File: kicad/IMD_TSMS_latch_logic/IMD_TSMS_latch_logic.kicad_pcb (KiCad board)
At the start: 2 copper layers, 32 parts, among them IC1 NE555, Q2 Q_PMOS_GDS, Q3 Q_PMOS_GDS, SW1 SW_Push, U1 4001, U2 4009, U3 4009, U4 4001

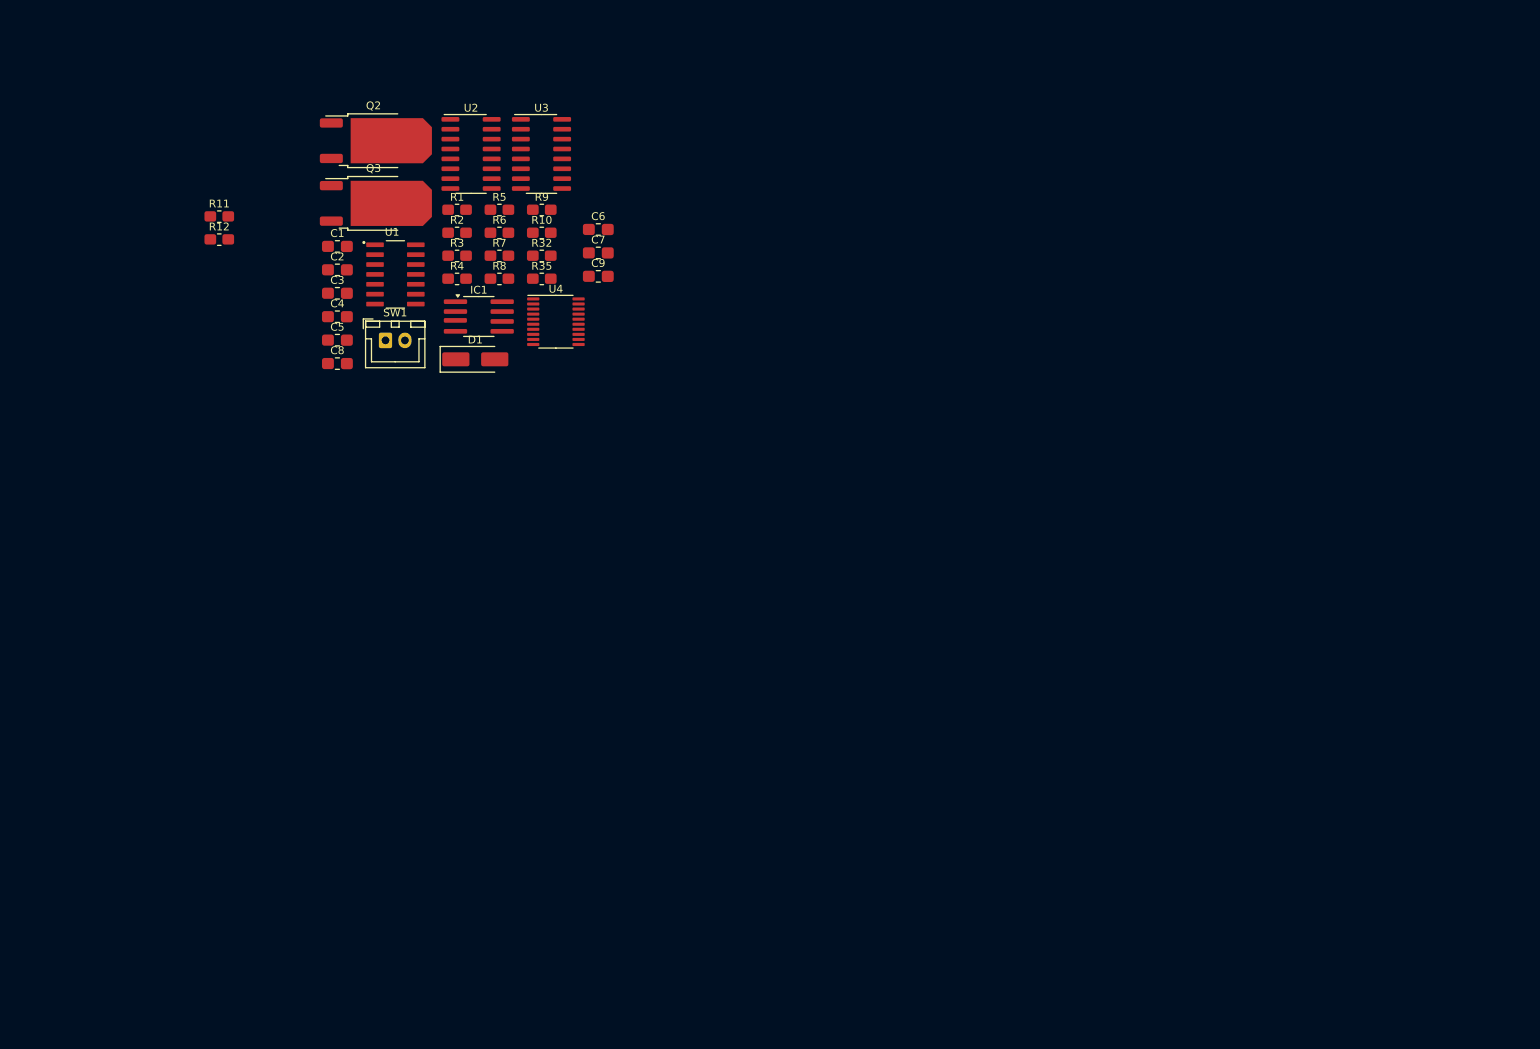
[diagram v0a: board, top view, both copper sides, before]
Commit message: Draw IMD latch
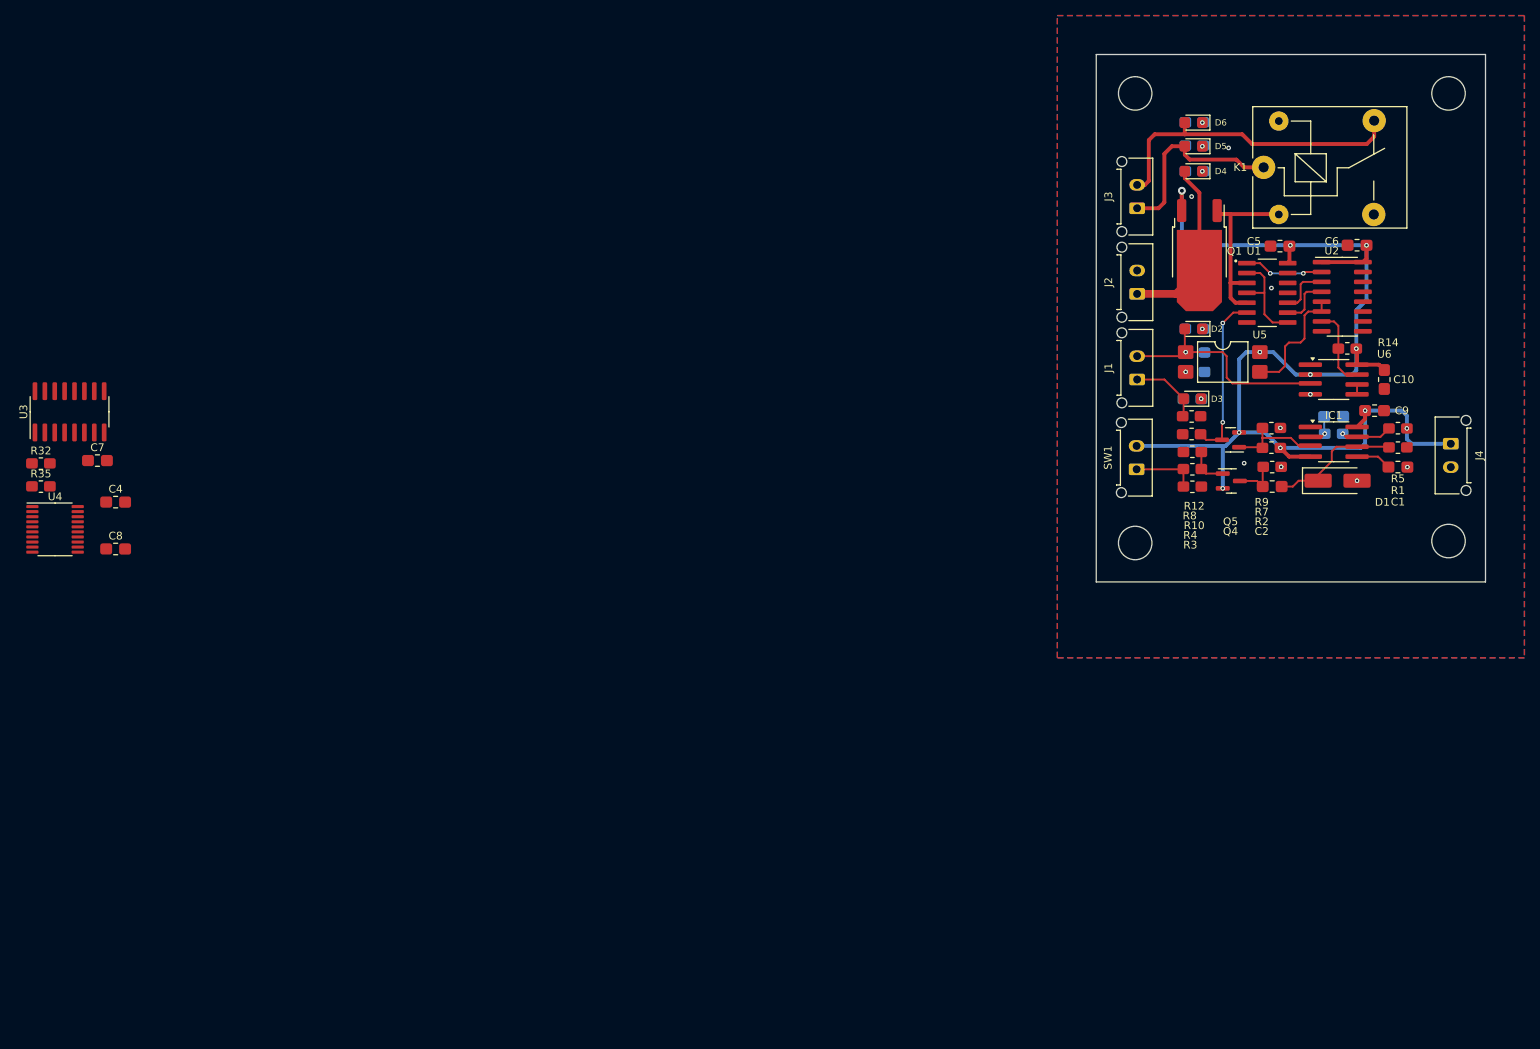
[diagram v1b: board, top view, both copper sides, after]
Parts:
- removed Q2, Q3: Q_PMOS_GDS, RMC_TO:TO-252-2
- added C10: 100nF, RMC_Capacitor:C_0805_2012Metric_Pad1.18x1.45mm_HandSolder_L, F.Cu at (187.0, 61.8)
- added D2: LED, RMC_LED:LED_0805_2012Metric_Pad1.45x1.40mm_HandSolder, F.Cu at (162.5, 55.2)
- added D3: LED, RMC_LED:LED_0805_2012Metric_Pad1.45x1.40mm_HandSolder, F.Cu at (162.3, 64.2)
- added D4: LED, RMC_LED:LED_0805_2012Metric_Pad1.45x1.40mm_HandSolder, F.Cu at (162.5, 35.0)
- added D5: LED, RMC_LED:LED_0805_2012Metric_Pad1.45x1.40mm_HandSolder, F.Cu at (162.5, 31.8)
- added D6: LED, RMC_LED:LED_0805_2012Metric_Pad1.45x1.40mm_HandSolder, F.Cu at (162.5, 28.8)
- added H1: MountingHole, MountingHole:MountingHole_4.3mm_M4, F.Cu at (195.2, 25.0)
- added H2: MountingHole, MountingHole:MountingHole_4.3mm_M4, F.Cu at (195.2, 82.5)
- added H3: MountingHole, MountingHole:MountingHole_4.3mm_M4, F.Cu at (155.0, 82.8)
- added H4: MountingHole, MountingHole:MountingHole_4.3mm_M4, F.Cu at (155.0, 25.0)
- added J1: Conn_01x02, Connector_Molex:Molex_Micro-Fit_3.0_43650-0215_1x02_P3.00mm_Vertical, F.Cu at (155.2, 61.8)
- added J2: Conn_01x02, Connector_Molex:Molex_Micro-Fit_3.0_43650-0215_1x02_P3.00mm_Vertical, F.Cu at (155.2, 50.8)
- added J3: Conn_01x02, Connector_Molex:Molex_Micro-Fit_3.0_43650-0215_1x02_P3.00mm_Vertical, F.Cu at (155.2, 39.8)
- added J4: Conn_01x02, Connector_Molex:Molex_Micro-Fit_3.0_43650-0215_1x02_P3.00mm_Vertical, F.Cu at (195.5, 70.0)
- added K1: SANYOU_SRD_Form_C, Relay_THT:Relay_SPDT_SANYOU_SRD_Series_Form_C, F.Cu at (171.5, 34.5)
- added Q1: Q_PMOS_GDS, RMC_TO:TO-252-2, F.Cu at (163.2, 45.5)
- added Q4: AO3401A, RMC_SOT:SOT-23, F.Cu at (167.3, 74.8)
- added Q5: AO3401A, RMC_SOT:SOT-23, F.Cu at (167.2, 69.5)
- added R13: 1k, RMC_Resistor:R_0805_2012Metric_Pad1.20x1.40mm_HandSolder_L, B.Cu at (162.8, 60.8)
- added R14: 1k, RMC_Resistor:R_0805_2012Metric_Pad1.20x1.40mm_HandSolder_L, F.Cu at (182.2, 57.8)
- added R15: 1k, RMC_Resistor:R_0805_2012Metric_Pad1.20x1.40mm_HandSolder_L, B.Cu at (162.6, 55.2)
- added R16: 1k, RMC_Resistor:R_0805_2012Metric_Pad1.20x1.40mm_HandSolder_L, B.Cu at (162.3, 64.2)
- added R17: 1k, RMC_Resistor:R_0805_2012Metric_Pad1.20x1.40mm_HandSolder_L, B.Cu at (162.6, 35.0)
- added R18: 1k, RMC_Resistor:R_0805_2012Metric_Pad1.20x1.40mm_HandSolder_L, B.Cu at (162.6, 31.7)
- added R19: 1k, RMC_Resistor:R_0805_2012Metric_Pad1.20x1.40mm_HandSolder_L, B.Cu at (162.6, 28.7)
- added U5: LTV-817S, Package_DIP:SMDIP-4_W9.53mm, F.Cu at (166.2, 59.5)
- added U6: LM311, RMC_SO:SOIC-8_3.9x4.9mm_P1.27mm_RMC_Handsolder, F.Cu at (180.5, 61.8)
- C3, R11, R6: moved to B.Cu
- SW1: footprint Connector_JST:JST_XH_B2B-XH-A_1x02_P2.50mm_Vertical -> Connector_Molex:Molex_Micro-Fit_3.0_43650-0215_1x02_P3.00mm_Vertical
- moved C1 139.1 mm to (188.8, 73.0)
- moved C3 129.0 mm to (180.5, 66.5)
- moved R12 127.0 mm to (162.2, 66.5)
- moved R11 126.6 mm to (162.8, 58.2)
- moved R1 124.7 mm to (188.8, 70.5)
- moved C2 123.3 mm to (172.6, 75.5)
- moved C5 121.7 mm to (173.6, 44.6), turned to 180 degrees
- moved R5 118.8 mm to (188.8, 68.0), turned to 180 degrees
- moved U2 113.4 mm to (181.6, 51.1)
- moved U1 112.0 mm to (172.0, 50.6)
- moved D1 111.9 mm to (181.0, 74.8)
- moved IC1 111.0 mm to (180.5, 69.8)
- moved R6 110.2 mm to (180.5, 68.8), turned to 180 degrees
- moved R2 108.9 mm to (172.6, 73.0)
- moved R7 102.2 mm to (172.5, 70.5), turned to 180 degrees
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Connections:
- net /IMD_latch_output renamed Net-(U1-Pad2)
- net Net-(U1-Pad3) renamed IMD_RELAY
- R12 pad 1: IMD_MHs -> /IMD_MHs
- U2 pad 5: /IMD_OKHs -> /OKHs_logic
- U2 pad 6: unconnected-(U2-Pad6) -> /OKHs_logic
- U2 pad 7: unconnected-(U2-Pad7) -> Net-(R14-Pad2)
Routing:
- net +12V: track 0.00 -> 153.7 mm, vias 0 -> 11
- net /SDC_OUT: track 0.00 -> 40.7 mm
- net /IMD_OKHs: track 0.00 -> 28.9 mm, vias 0 -> 1
- net IMD_LED: track 0.00 -> 25.1 mm
- net /SDC_IN: track 0.00 -> 25.0 mm
- net IMD_RELAY: track 0.00 -> 24.6 mm
- net /IMD_reset: track 0.00 -> 21.7 mm, vias 0 -> 2
- net /THRES: track 0.00 -> 17.1 mm
- net /OKHs_logic: track 0.00 -> 15.6 mm
- net Net-(U1-Pad2): track 0.00 -> 12.9 mm
- net /fall_edge_out: track 0.00 -> 12.2 mm
- net Net-(R14-Pad2): track 0.00 -> 10.5 mm
- net Net-(U1-Pad1): track 0.00 -> 10.2 mm, vias 0 -> 2
- net /IMD_MHs: track 0.00 -> 9.30 mm
- net Net-(R3-Pad1): track 0.00 -> 8.28 mm
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- added copper zone on B.Cu, net GND
- added copper zone on F.Cu, net GND
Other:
- board outline added: 50 x 67.8 mm

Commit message: IMD latch with small IMD moutning
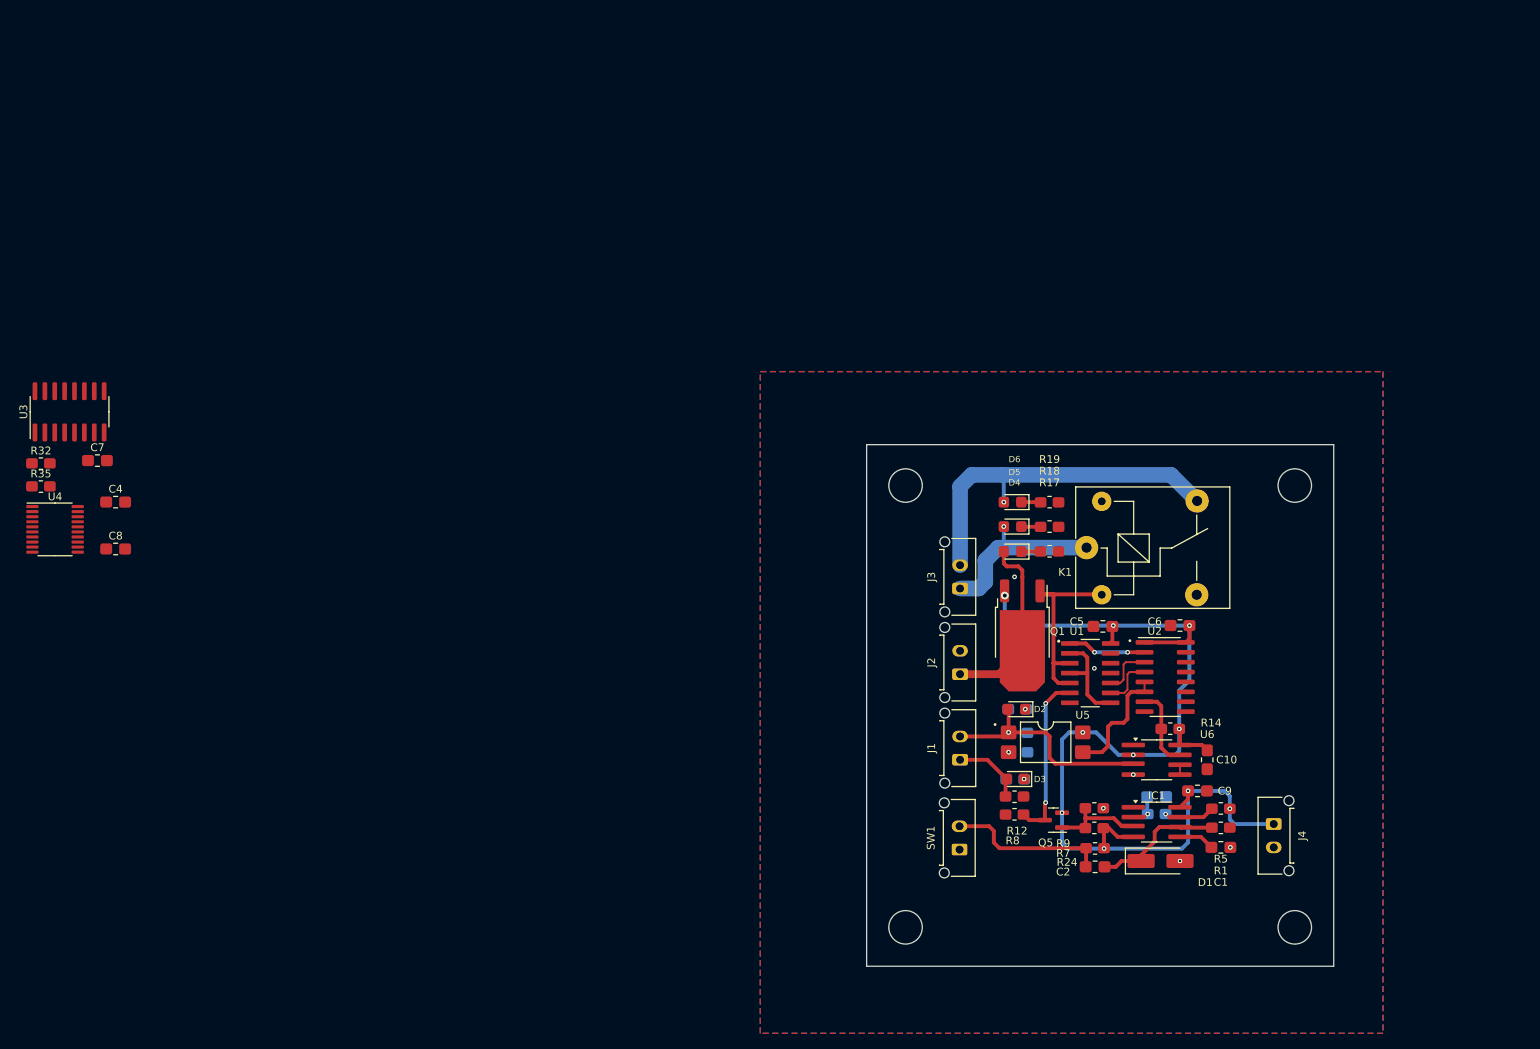
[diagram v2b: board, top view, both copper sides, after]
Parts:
- removed Q4: AO3401A, RMC_SOT:SOT-23
- removed R10: 100k, RMC_Resistor:R_0805_2012Metric_Pad1.20x1.40mm_HandSolder_L
- removed R2: 10k, RMC_Resistor:R_0805_2012Metric_Pad1.20x1.40mm_HandSolder_L
- removed R3, R4: 1k, RMC_Resistor:R_0805_2012Metric_Pad1.20x1.40mm_HandSolder_L
- added R24: 10k, RMC_Resistor:R_0805_2012Metric_Pad1.20x1.40mm_HandSolder_L, F.Cu at (149.8, 122.0)
- R17, R18, R19: moved to F.Cu
- moved H1 108.9 mm to (175.5, 132.1), turned to -90 degrees
- moved H2 85.6 mm to (125.5, 132.1), turned to -90 degrees
- moved H4 54.4 mm to (175.5, 75.4), turned to -90 degrees
- moved D5 54.1 mm to (139.2, 80.6)
- moved D4 54.1 mm to (139.2, 83.8)
- moved D6 54.0 mm to (139.2, 77.5)
- moved C5 53.9 mm to (150.9, 93.5)
- moved U1 53.9 mm to (149.2, 99.5)
- moved U2 53.9 mm to (158.9, 100.0)
- moved C1 53.9 mm to (166.0, 121.8)
- moved C10 53.9 mm to (164.3, 110.6)
- moved C2 53.9 mm to (149.9, 124.3)
- moved C3 53.9 mm to (157.8, 115.3)
- moved C6 53.9 mm to (160.8, 93.3)
- moved C9 53.9 mm to (163.0, 114.6)
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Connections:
- C2 pad 1: Net-(Q4-D) -> Net-(C2-Pad1)
- SW1 pad 1: Net-(R3-Pad1) -> GND
- SW1 pad 2: +12V -> Net-(C2-Pad1)
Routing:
- net Net-(C2-Pad1): track 0.00 -> 20.7 mm
- net +12V: track 153.7 -> 137.2 mm, vias 11 -> 10
- net Net-(R3-Pad1): track 8.28 -> 0.00 mm
- net Net-(Q4-D): track 5.78 -> 0.00 mm
- net /SDC_OUT: track 40.7 -> 46.1 mm, vias 0 -> 1
- net Net-(Q4-G): track 5.17 -> 0.00 mm
- net /fall_edge_out: track 12.2 -> 14.7 mm
- net Net-(D4-K): track 0.12 -> 2.47 mm, vias 1 -> 0
- net Net-(D6-K): track 0.14 -> 2.49 mm, vias 1 -> 0
- net Net-(D5-K): track 0.16 -> 2.49 mm, vias 1 -> 0
- net /SDC_IN: track 25.0 -> 22.8 mm, vias 0 -> 1
- net IMD_LED: track 25.1 -> 23.9 mm
- net GND: vias 9 -> 6
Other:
- board size 50 x 67.8 mm -> 60 x 67 mm

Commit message: did all 3 boards
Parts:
- removed J2: Conn_01x02, Connector_Molex:Molex_Micro-Fit_3.0_43650-0215_1x02_P3.00mm_Vertical
- removed Q1: Q_PMOS_GDS, RMC_TO:TO-252-2
- added D7: LED, RMC_LED:LED_0805_2012Metric_Pad1.45x1.40mm_HandSolder, F.Cu at (92.8, 85.7)
- added H10: MountingHole, MountingHole:MountingHole_4.3mm_M4, F.Cu at (115.0, 75.4)
- added H11: MountingHole, MountingHole:MountingHole_4.3mm_M4, F.Cu at (80.0, 85.0)
- added H12: MountingHole, MountingHole:MountingHole_4.3mm_M4, F.Cu at (115.0, 85.0)
- added H5: MountingHole, MountingHole:MountingHole_4.3mm_M4, F.Cu at (115.0, 132.0)
- added H6: MountingHole, MountingHole:MountingHole_4.3mm_M4, F.Cu at (115.0, 96.0)
- added H7: MountingHole, MountingHole:MountingHole_4.3mm_M4, F.Cu at (80.0, 132.0)
- added H8: MountingHole, MountingHole:MountingHole_4.3mm_M4, F.Cu at (80.0, 75.4)
- added H9: MountingHole, MountingHole:MountingHole_4.3mm_M4, F.Cu at (80.0, 96.0)
- added J5: Conn_01x02, Connector_Molex:Molex_Micro-Fit_3.0_43650-0215_1x02_P3.00mm_Vertical, F.Cu at (90.8, 78.0)
- added J6: Conn_01x02, Connector_Molex:Molex_Micro-Fit_3.0_43650-0215_1x02_P3.00mm_Vertical, F.Cu at (102.0, 78.0)
- added J7: Conn_01x02, Connector_Molex:Molex_Micro-Fit_3.0_43650-0215_1x02_P3.00mm_Vertical, F.Cu at (132.5, 99.8)
- added J8: Conn_01x02, Connector_Molex:Molex_Micro-Fit_3.0_43650-0215_1x02_P3.00mm_Vertical, F.Cu at (106.4, 114.5)
- added J9: Conn_01x02, Connector_Molex:Molex_Micro-Fit_3.0_43650-0215_1x02_P3.00mm_Vertical, F.Cu at (106.4, 125.8)
- added K2: SANYOU_SRD_Form_C, Relay_THT:Relay_SPDT_SANYOU_SRD_Series_Form_C, F.Cu at (93.5, 114.0)
- added Q2: AO3400A, RMC_SOT:SOT-23, F.Cu at (98.0, 84.2)
- added Q3: AO3401A, RMC_SOT:SOT-23, F.Cu at (90.2, 106.6)
- added Q6: AO3401A, RMC_SOT:SOT-23, F.Cu at (139.8, 96.2)
- added R10: 100k, RMC_Resistor:R_0805_2012Metric_Pad1.20x1.40mm_HandSolder_L, F.Cu at (139.8, 101.5)
- added R2: 1k, RMC_Resistor:R_0805_2012Metric_Pad1.20x1.40mm_HandSolder_L, F.Cu at (154.8, 106.8)
- added R20: 1k, RMC_Resistor:R_0805_2012Metric_Pad1.20x1.40mm_HandSolder_L, F.Cu at (104.2, 84.7)
- added R21: 1k, RMC_Resistor:R_0805_2012Metric_Pad1.20x1.40mm_HandSolder_L, F.Cu at (92.8, 83.2)
- added R22: JUMPER, RMC_Resistor:R_0805_2012Metric_Pad1.20x1.40mm_HandSolder_L, F.Cu at (145.2, 89.2)
- added R23: 1k, RMC_Resistor:R_0805_2012Metric_Pad1.20x1.40mm_HandSolder_L, F.Cu at (149.8, 116.8)
- added R25: 1k, RMC_Resistor:R_0805_2012Metric_Pad1.20x1.40mm_HandSolder_L, F.Cu at (139.8, 99.2)
- added R26: 1k, RMC_Resistor:R_0805_2012Metric_Pad1.20x1.40mm_HandSolder_L, F.Cu at (92.2, 102.9)
- added R27: 100k, RMC_Resistor:R_0805_2012Metric_Pad1.20x1.40mm_HandSolder_L, F.Cu at (93.4, 106.6)
- added R28: 1k, RMC_Resistor:R_0805_2012Metric_Pad1.20x1.40mm_HandSolder_L, F.Cu at (92.2, 110.2)
- added R3: 1k, RMC_Resistor:R_0805_2012Metric_Pad1.20x1.40mm_HandSolder_L, F.Cu at (139.8, 93.2)
- added R4: 100k, RMC_Resistor:R_0805_2012Metric_Pad1.20x1.40mm_HandSolder_L, F.Cu at (101.8, 84.7)
- C8: footprint RMC_Capacitor:C_0805_2012Metric_Pad1.18x1.45mm_HandSolder_L -> RMC_Capacitor:CP_Radial_D6.3mm_P2.50mm_extended
- U4: footprint RMC_SO:TSSOP-20_4.4x6.5mm_P0.65mm -> RMC_SO:SOIC127P600X175-14N
- moved C7 93.4 mm to (108.0, 108.0), turned to -90 degrees
- moved U3 92.1 mm to (101.0, 106.0), turned to -90 degrees
- moved U4 86.8 mm to (101.8, 96.2), turned to -90 degrees
- moved C4 86.3 mm to (108.0, 97.5), turned to 90 degrees
- moved R32 80.1 mm to (87.0, 106.5), turned to -90 degrees
- moved R35 77.1 mm to (87.0, 101.5), turned to 90 degrees
- moved C8 70.0 mm to (92.5, 98.0), turned to 90 degrees
- moved R9 2.13 mm to (149.8, 114.7)
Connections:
- Q5 pad 1: /fall_edge_out -> Net-(Q5-G)
- R7 pad 2: /fall_edge_out -> Net-(Q5-G)
- R9 pad 1: /fall_edge_out -> Net-(Q5-G)
- U1 pad 3: IMD_RELAY -> /IMD_latch_output
- U1 pad 5: IMD_RELAY -> /IMD_latch_output
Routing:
- net +12V: track 137.2 -> 206.0 mm, vias 10 -> 12
- net /TSMS_input: track 0.00 -> 37.2 mm
- net /TSMS_latch_output: track 0.00 -> 23.1 mm
- net /TSMS_reset: track 0.00 -> 22.3 mm
- net IMD_RELAY: track 24.6 -> 44.7 mm
- net /IMD_latch_output: track 0.00 -> 18.3 mm
- net Net-(Q3-D): track 0.00 -> 16.6 mm
- net Net-(U3-Pad2): track 0.00 -> 10.3 mm, vias 0 -> 2
- net /fall_edge_out: track 14.7 -> 4.76 mm
- net Net-(Q5-G): track 0.00 -> 7.73 mm
- net /TSMS_output: track 0.00 -> 7.14 mm
- net Net-(U3-Pad3): track 0.00 -> 6.36 mm
- net Net-(U4-Pad3): track 0.00 -> 6.12 mm
- net Net-(Q6-G): track 0.00 -> 6.11 mm
- net Net-(U3-Pad4): track 0.00 -> 6.08 mm
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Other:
- board size 60 x 67 mm -> 105.5 x 67 mm
